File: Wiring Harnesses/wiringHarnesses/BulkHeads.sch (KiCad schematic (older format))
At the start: 0 parts

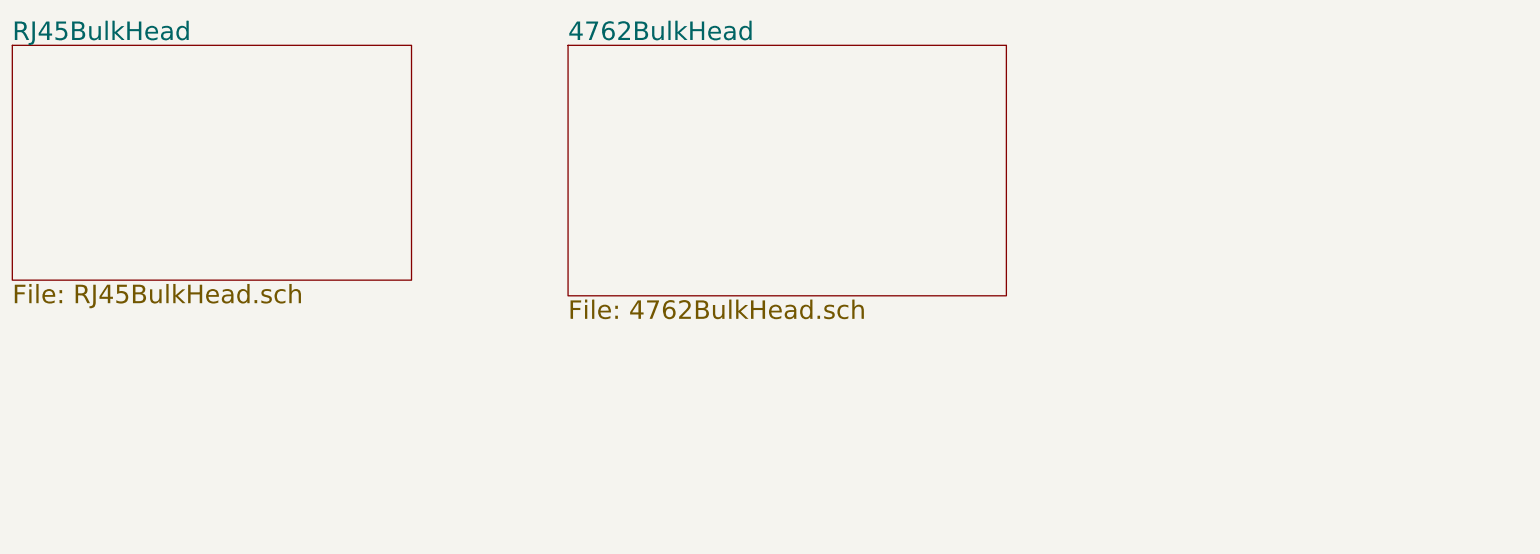
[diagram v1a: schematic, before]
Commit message: Added node power cables and skeleton for other power cables
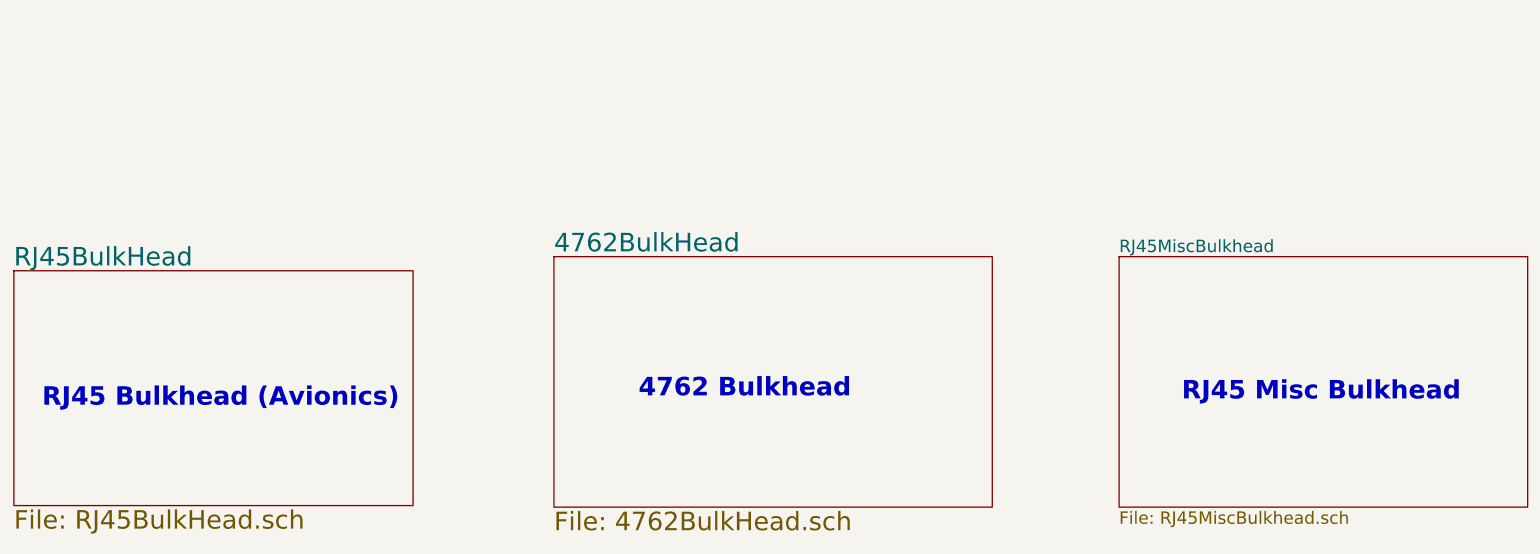
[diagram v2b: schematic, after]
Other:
- note added: "4762 Bulkhead\n"
- note added: "RJ45 Bulkhead (Avionics)"
- note added: "RJ45 Misc Bulkhead"
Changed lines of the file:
@@
 $Descr A4 11693 8268
 encoding utf-8
-Sheet 10 14
+Sheet 12 20
 Title ""
 Date ""
@@
 $EndDescr
 $Sheet
-S 1150 1350 2550 1500
+S 1160 2790 2550 1500
 U 5CD2F05E
 F0 "RJ45BulkHead" 118
@@
 $EndSheet
 $Sheet
-S 4700 1350 2800 1600
+S 4610 2700 2800 1600
 U 5CD2F063
 F0 "4762BulkHead" 118
 F1 "4762BulkHead.sch" 118
 $EndSheet
+Text Notes 1340 3670 0    118  ~ 24
+RJ45 Bulkhead (Avionics)
+Text Notes 5150 3610 0    118  ~ 24
+4762 Bulkhead\n
+$Sheet
+S 8220 2700 2610 1600
+U 5CD47BDF
+F0 "RJ45MiscBulkhead" 79
+F1 "RJ45MiscBulkhead.sch" 79
+$EndSheet
+Text Notes 8620 3630 0    118  ~ 24
+RJ45 Misc Bulkhead
 $EndSCHEMATC

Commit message: Added some bulkheads and internal HV connectors
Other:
- note added: "RJ45 (Motor)\n"
- note removed: "RJ45 Misc Bulkhead"
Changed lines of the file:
@@
 $Descr A4 11693 8268
 encoding utf-8
-Sheet 12 20
+Sheet 11 20
 Title ""
 Date ""
@@
 F1 "RJ45MiscBulkhead.sch" 79
 $EndSheet
-Text Notes 8620 3630 0    118  ~ 24
-RJ45 Misc Bulkhead
+Text Notes 8800 3650 0    118  ~ 24
+RJ45 (Motor)\n
 $EndSCHEMATC

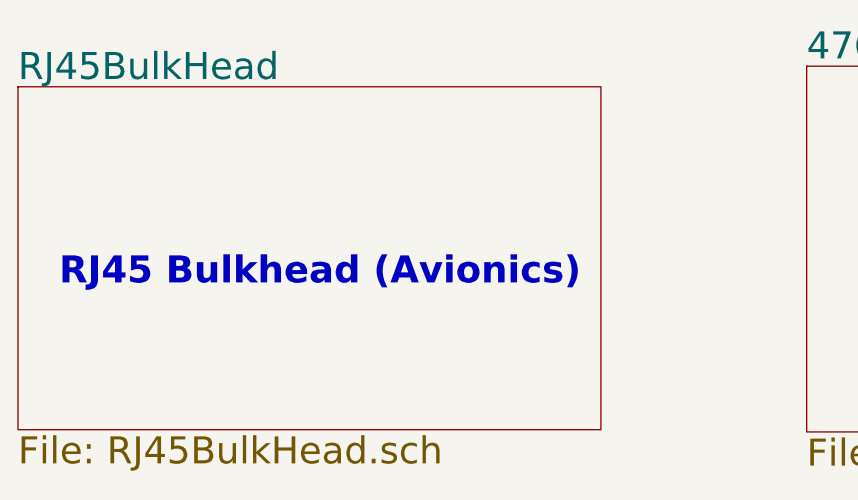
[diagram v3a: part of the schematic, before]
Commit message: added 1872 bulkhead
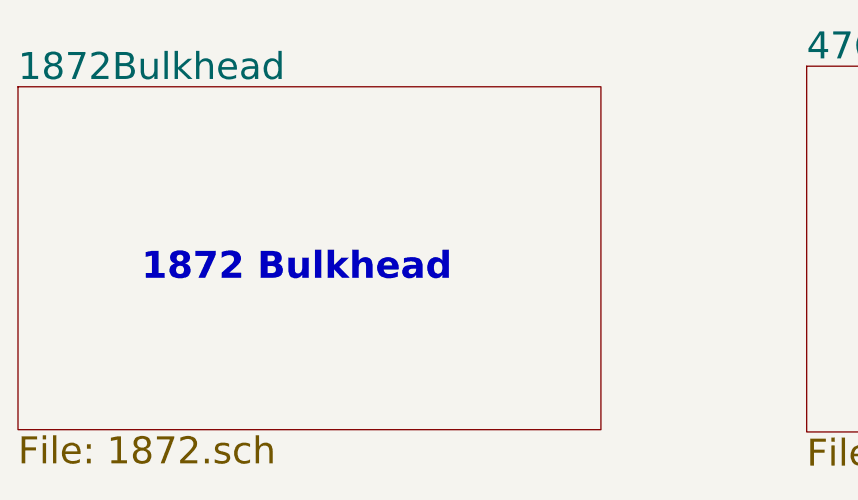
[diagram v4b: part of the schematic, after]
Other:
- note added: "1872 Bulkhead\n"
- note removed: "RJ45 Bulkhead (Avionics)"
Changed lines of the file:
@@
 $EndDescr
-$Sheet
-S 1160 2790 2550 1500
-U 5CD2F05E
-F0 "RJ45BulkHead" 118
-F1 "RJ45BulkHead.sch" 118
-$EndSheet
 $Sheet
 S 4610 2700 2800 1600
@@
 F1 "4762BulkHead.sch" 118
 $EndSheet
-Text Notes 1340 3670 0    118  ~ 24
-RJ45 Bulkhead (Avionics)
+Text Notes 1700 3650 0    118  ~ 24
+1872 Bulkhead\n
 Text Notes 5150 3610 0    118  ~ 24
 4762 Bulkhead\n
@@
 Text Notes 8800 3650 0    118  ~ 24
 RJ45 (Motor)\n
+$Sheet
+S 1160 2790 2550 1500
+U 5CD2F05E
+F0 "1872Bulkhead" 118
+F1 "1872.sch" 118
+$EndSheet
 $EndSCHEMATC
